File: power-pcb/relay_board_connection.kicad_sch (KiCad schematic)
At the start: 17 parts, among them J1 RA25S

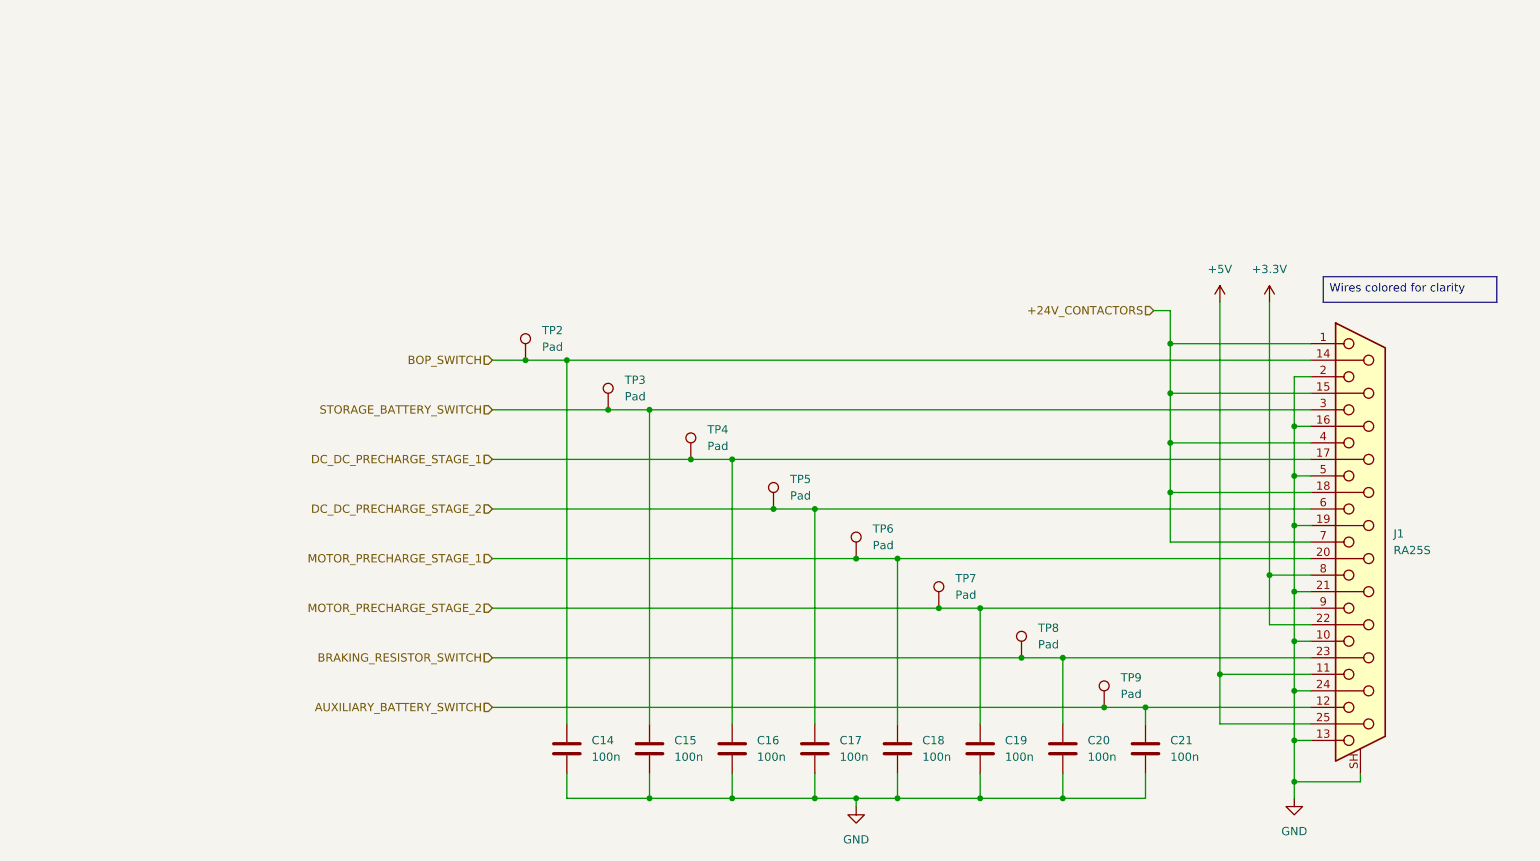
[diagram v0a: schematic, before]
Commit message: power-pcb: finish schematic pages 1 to 7
- overview
- non-isolated interfaces + power
- stm32 microcontroller
- relay board connection
- battery sensors
- 48v i-v sensing (x2)
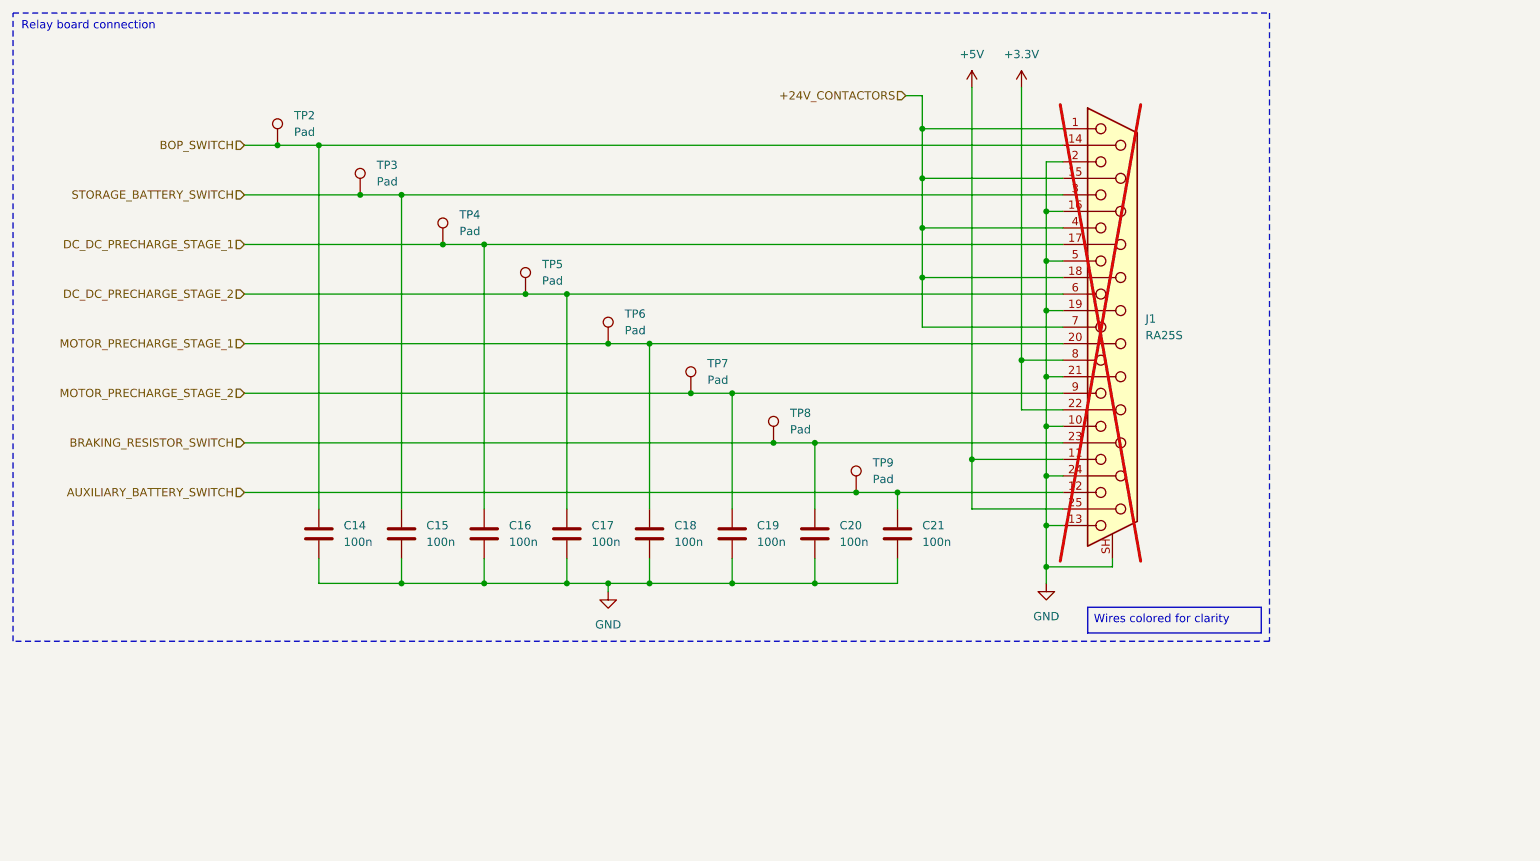
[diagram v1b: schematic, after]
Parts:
- J1: now not fitted
- TP2, TP3, TP4, TP5, TP6, TP7, TP8, TP9: now left out of the parts list
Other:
- note added: "Relay board connection"
- moved on the sheet: C14, C15, C16, C17, C18, C19, C20, C21, TP2, TP3, TP4, TP5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

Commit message: power-pcb: finish schematic layout
All parts are placed and connected, ERC passes (except for two
exclusions with comment).
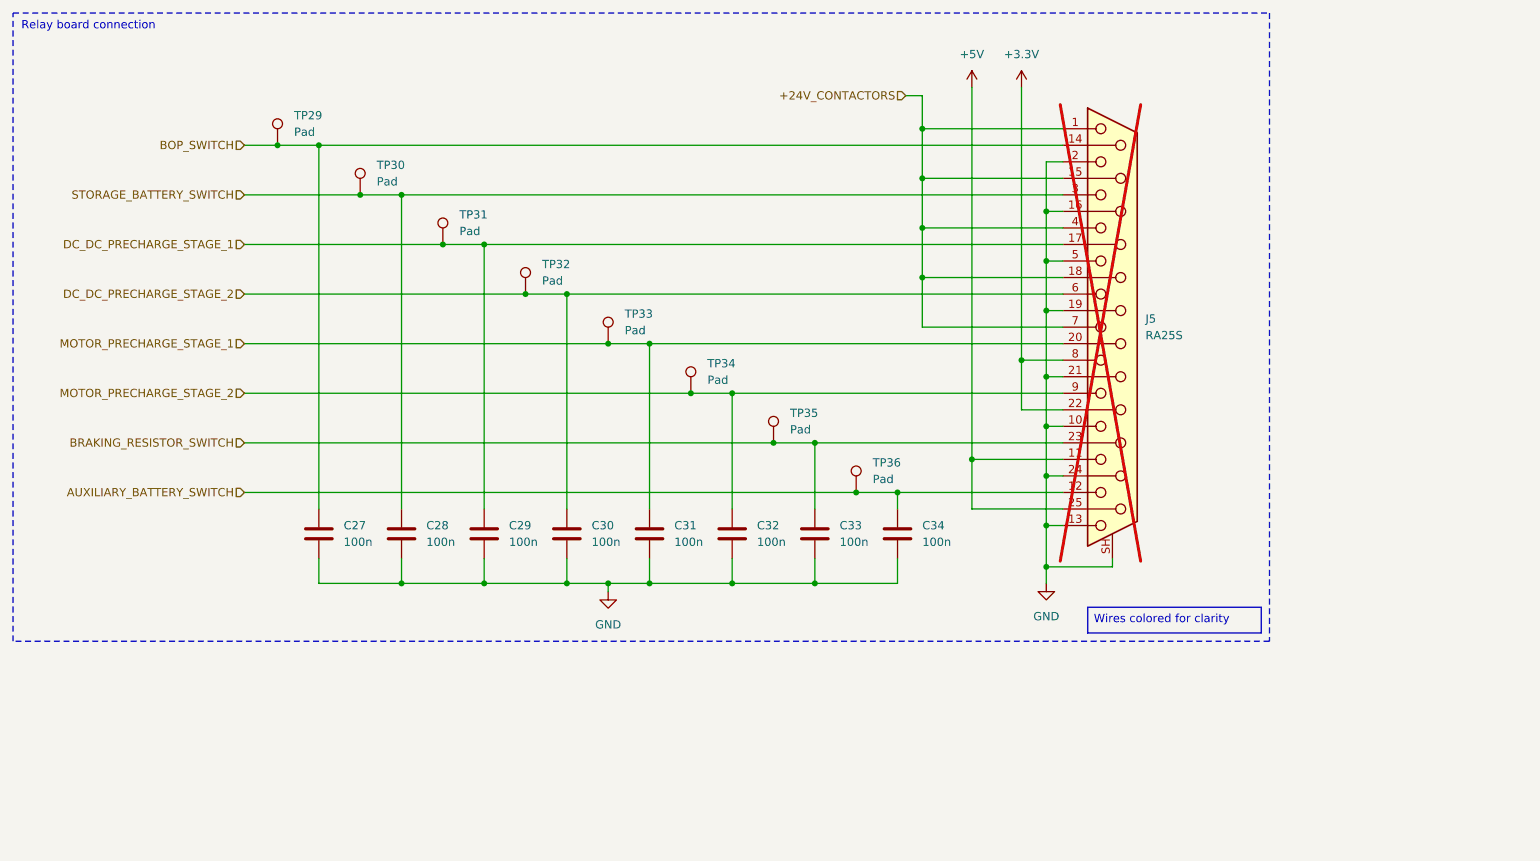
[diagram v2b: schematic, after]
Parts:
- renumbered C14 to C27, C15 to C28, C16 to C29, C17 to C30, C18 to C31, C19 to C32, C20 to C33, C21 to C34, J1 to J5, TP2 to TP29, TP3 to TP30, TP4 to TP31, TP5 to TP32, TP6 to TP33, TP7 to TP34, TP8 to TP35, TP9 to TP36
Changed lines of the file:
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@@
 	(title_block
 		(title "Relay Board Connection")
-		(date "2026-05-31")
+		(date "2026-06-13")
 		(rev "v1.1.0")
 	)
@@
 		(dnp no)
 		(fields_autoplaced yes)
-		(property "Reference" "C20"
+		(property "Reference" "C33"
 			(at 139.7 91.4399 0)
 			(show_name no)
@@
 			(project "power-pcb"
 				(path "/4b4cf3aa-c94c-4150-b9c5-35049cd71136/9838bcc9-e766-495a-ad52-0ec70b90713f"
-					(reference "C20")
+					(reference "C33")
 					(unit 1)
+					(variant
+						(name "JLCPCB")
+					)
 				)
 			)
@@
 		(dnp no)
 		(fields_autoplaced yes)
-		(property "Reference" "C16"
+		(property "Reference" "C29"
 			(at 88.9 91.4399 0)
 			(show_name no)
@@
 			(project "power-pcb"
 				(path "/4b4cf3aa-c94c-4150-b9c5-35049cd71136/9838bcc9-e766-495a-ad52-0ec70b90713f"
-					(reference "C16")
+					(reference "C29")
 					(unit 1)
+					(variant
+						(name "JLCPCB")
+					)
 				)
 			)
@@
 		(dnp no)
 		(fields_autoplaced yes)
-		(property "Reference" "#PWR020"
+		(property "Reference" "#PWR058"
 			(at 104.14 107.95 0)
 			(hide yes)
@@
 			(project "power-pcb"
 				(path "/4b4cf3aa-c94c-4150-b9c5-35049cd71136/9838bcc9-e766-495a-ad52-0ec70b90713f"
-					(reference "#PWR020")
+					(reference "#PWR058")
 					(unit 1)
 				)
@@
 		(dnp no)
 		(fields_autoplaced yes)
-		(property "Reference" "TP3"
+		(property "Reference" "TP30"
 			(at 68.58 36.0679 0)
 			(show_name no)
@@
 			(project "power-pcb"
 				(path "/4b4cf3aa-c94c-4150-b9c5-35049cd71136/9838bcc9-e766-495a-ad52-0ec70b90713f"
-					(reference "TP3")
+					(reference "TP30")
 					(unit 1)
+					(variant
+						(name "JLCPCB")
+					)
 				)
 			)
@@
 		(dnp no)
 		(fields_autoplaced yes)
-		(property "Reference" "C17"
+		(property "Reference" "C30"
 			(at 101.6 91.4399 0)
 			(show_name no)
@@
 			(project "power-pcb"
 				(path "/4b4cf3aa-c94c-4150-b9c5-35049cd71136/9838bcc9-e766-495a-ad52-0ec70b90713f"
-					(reference "C17")
+					(reference "C30")
 					(unit 1)
+					(variant
+						(name "JLCPCB")
+					)
 				)
 			)
@@
 		(dnp no)
 		(fields_autoplaced yes)
-		(property "Reference" "#PWR023"
+		(property "Reference" "#PWR057"
 			(at 171.45 106.68 0)
 			(hide yes)
@@
 			(project "power-pcb"
 				(path "/4b4cf3aa-c94c-4150-b9c5-35049cd71136/9838bcc9-e766-495a-ad52-0ec70b90713f"
-					(reference "#PWR023")
+					(reference "#PWR057")
 					(unit 1)
 				)
@@
 		(dnp no)
 		(fields_autoplaced yes)
-		(property "Reference" "TP2"
+		(property "Reference" "TP29"
 			(at 55.88 28.4479 0)
 			(show_name no)
@@
 			(project "power-pcb"
 				(path "/4b4cf3aa-c94c-4150-b9c5-35049cd71136/9838bcc9-e766-495a-ad52-0ec70b90713f"
-					(reference "TP2")
+					(reference "TP29")
 					(unit 1)
+					(variant
+						(name "JLCPCB")
+					)
 				)
 			)
@@
 		(dnp no)
 		(fields_autoplaced yes)
-		(property "Reference" "TP9"
+		(property "Reference" "TP36"
 			(at 144.78 81.7879 0)
 			(show_name no)
@@
 			(project "power-pcb"
 				(path "/4b4cf3aa-c94c-4150-b9c5-35049cd71136/9838bcc9-e766-495a-ad52-0ec70b90713f"
-					(reference "TP9")
+					(reference "TP36")
 					(unit 1)
+					(variant
+						(name "JLCPCB")
+					)
 				)
 			)
@@
 		(dnp yes)
 		(fields_autoplaced yes)
-		(property "Reference" "J1"
+		(property "Reference" "J5"
 			(at 186.69 59.6899 0)
 			(show_name no)
@@
 			(project "power-pcb"
 				(path "/4b4cf3aa-c94c-4150-b9c5-35049cd71136/9838bcc9-e766-495a-ad52-0ec70b90713f"
-					(reference "J1")
+					(reference "J5")
 					(unit 1)
+					(variant
+						(name "JLCPCB")
+					)
 				)
 			)
@@
 		(dnp no)
 		(fields_autoplaced yes)
-		(property "Reference" "#PWR021"
+		(property "Reference" "#PWR055"
 			(at 160.02 27.94 0)
 			(hide yes)
@@
 			(project "power-pcb"
 				(path "/4b4cf3aa-c94c-4150-b9c5-35049cd71136/9838bcc9-e766-495a-ad52-0ec70b90713f"
-					(reference "#PWR021")
+					(reference "#PWR055")
 					(unit 1)
 				)
@@
 		(dnp no)
 		(fields_autoplaced yes)
-		(property "Reference" "#PWR022"
+		(property "Reference" "#PWR056"
 			(at 167.64 27.94 0)
 			(hide yes)
@@
 			(project "power-pcb"
 				(path "/4b4cf3aa-c94c-4150-b9c5-35049cd71136/9838bcc9-e766-495a-ad52-0ec70b90713f"
-					(reference "#PWR022")
+					(reference "#PWR056")
 					(unit 1)
 				)
@@
 		(dnp no)
 		(fields_autoplaced yes)
-		(property "Reference" "TP8"
+		(property "Reference" "TP35"
 			(at 132.08 74.1679 0)
 			(show_name no)
@@
 			(project "power-pcb"
 				(path "/4b4cf3aa-c94c-4150-b9c5-35049cd71136/9838bcc9-e766-495a-ad52-0ec70b90713f"
-					(reference "TP8")
+					(reference "TP35")
 					(unit 1)
+					(variant
+						(name "JLCPCB")
+					)
 				)
 			)
@@
 		(dnp no)
 		(fields_autoplaced yes)
-		(property "Reference" "C21"
+		(property "Reference" "C34"
 			(at 152.4 91.4399 0)
 			(show_name no)
@@
 			(project "power-pcb"
 				(path "/4b4cf3aa-c94c-4150-b9c5-35049cd71136/9838bcc9-e766-495a-ad52-0ec70b90713f"
-					(reference "C21")
+					(reference "C34")
 					(unit 1)
+					(variant
+						(name "JLCPCB")
+					)
 				)
 			)
@@
 		(dnp no)
 		(fields_autoplaced yes)
-		(property "Reference" "TP6"
+		(property "Reference" "TP33"
 			(at 106.68 58.9279 0)
 			(show_name no)
@@
 			(project "power-pcb"
 				(path "/4b4cf3aa-c94c-4150-b9c5-35049cd71136/9838bcc9-e766-495a-ad52-0ec70b90713f"
-					(reference "TP6")
+					(reference "TP33")
 					(unit 1)
+					(variant
+						(name "JLCPCB")
+					)
 				)
 			)
@@
 		(dnp no)
 		(fields_autoplaced yes)
-		(property "Reference" "TP5"
+		(property "Reference" "TP32"
 			(at 93.98 51.3079 0)
 			(show_name no)
@@
 			(project "power-pcb"
 				(path "/4b4cf3aa-c94c-4150-b9c5-35049cd71136/9838bcc9-e766-495a-ad52-0ec70b90713f"
-					(reference "TP5")
+					(reference "TP32")
 					(unit 1)
+					(variant
+						(name "JLCPCB")
+					)
 				)
 			)
@@
 		(dnp no)
 		(fields_autoplaced yes)
-		(property "Reference" "C18"
+		(property "Reference" "C31"
 			(at 114.3 91.4399 0)
 			(show_name no)
@@
 			(project "power-pcb"
 				(path "/4b4cf3aa-c94c-4150-b9c5-35049cd71136/9838bcc9-e766-495a-ad52-0ec70b90713f"
-					(reference "C18")
+					(reference "C31")
 					(unit 1)
+					(variant
+						(name "JLCPCB")
+					)
 				)
 			)
@@
 		(dnp no)
 		(fields_autoplaced yes)
-		(property "Reference" "C19"
+		(property "Reference" "C32"
 			(at 127 91.4399 0)
 			(show_name no)
@@
 			(project "power-pcb"
 				(path "/4b4cf3aa-c94c-4150-b9c5-35049cd71136/9838bcc9-e766-495a-ad52-0ec70b90713f"
-					(reference "C19")
+					(reference "C32")
 					(unit 1)
+					(variant
+						(name "JLCPCB")
+					)
 				)
 			)
@@
 		(dnp no)
 		(fields_autoplaced yes)
-		(property "Reference" "TP7"
+		(property "Reference" "TP34"
 			(at 119.38 66.5479 0)
 			(show_name no)
@@
 			(project "power-pcb"
 				(path "/4b4cf3aa-c94c-4150-b9c5-35049cd71136/9838bcc9-e766-495a-ad52-0ec70b90713f"
-					(reference "TP7")
+					(reference "TP34")
 					(unit 1)
+					(variant
+						(name "JLCPCB")
+					)
 				)
 			)
@@
 		(dnp no)
 		(fields_autoplaced yes)
-		(property "Reference" "C15"
+		(property "Reference" "C28"
 			(at 76.2 91.4399 0)
 			(show_name no)
@@
 			(project "power-pcb"
 				(path "/4b4cf3aa-c94c-4150-b9c5-35049cd71136/9838bcc9-e766-495a-ad52-0ec70b90713f"
-					(reference "C15")
+					(reference "C28")
 					(unit 1)
+					(variant
+						(name "JLCPCB")
+					)
 				)
 			)
@@
 		(dnp no)
 		(fields_autoplaced yes)
-		(property "Reference" "TP4"
+		(property "Reference" "TP31"
 			(at 81.28 43.6879 0)
 			(show_name no)
@@
 			(project "power-pcb"
 				(path "/4b4cf3aa-c94c-4150-b9c5-35049cd71136/9838bcc9-e766-495a-ad52-0ec70b90713f"
-					(reference "TP4")
+					(reference "TP31")
 					(unit 1)
+					(variant
+						(name "JLCPCB")
+					)
 				)
 			)
@@
 		(dnp no)
 		(fields_autoplaced yes)
-		(property "Reference" "C14"
+		(property "Reference" "C27"
 			(at 63.5 91.4399 0)
 			(show_name no)
@@
 			(project "power-pcb"
 				(path "/4b4cf3aa-c94c-4150-b9c5-35049cd71136/9838bcc9-e766-495a-ad52-0ec70b90713f"
-					(reference "C14")
+					(reference "C27")
 					(unit 1)
-				)
-			)
+					(variant
+						(name "JLCPCB")
+					)
+				)
+			)

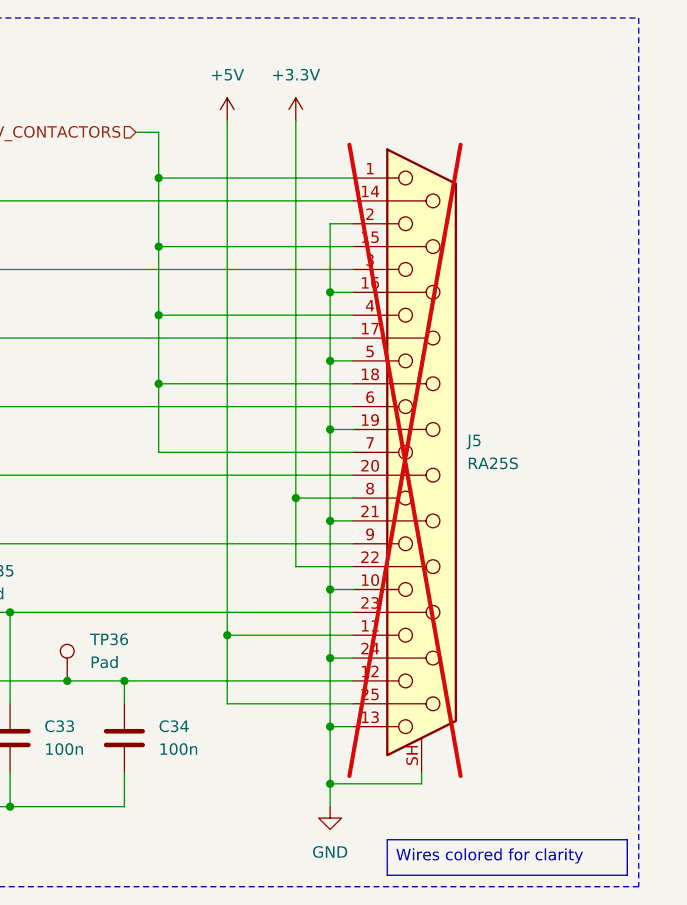
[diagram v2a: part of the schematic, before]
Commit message: power-pcb: finish assigning JLCPCB PN
Also assigned missing footprints.
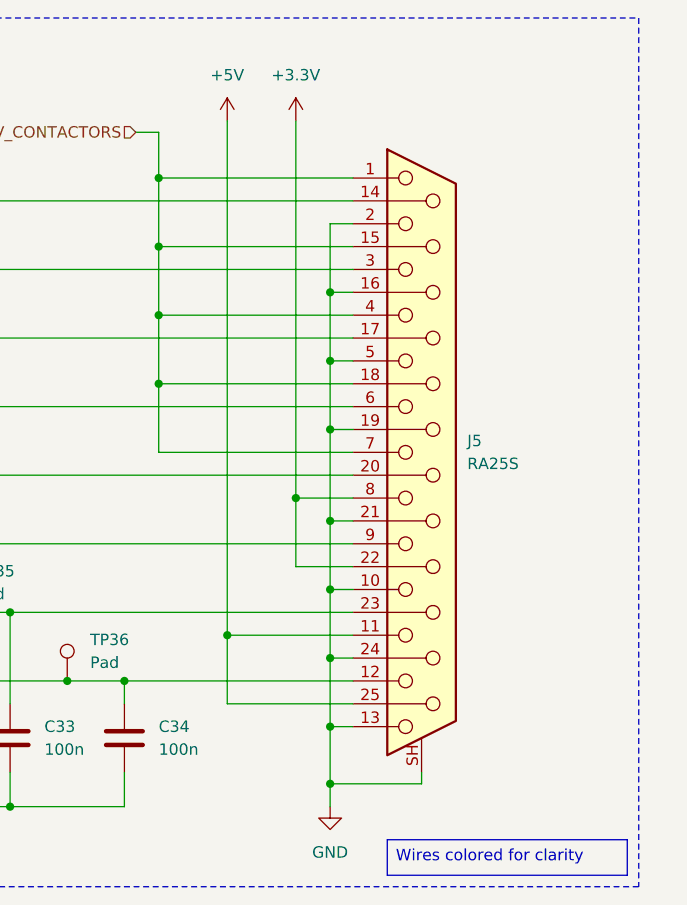
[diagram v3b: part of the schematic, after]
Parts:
- J5: MFR (none) -> Assmann WSW Components; MPN (none) -> A-DF 25 A/KG-T2S; now fitted
- TP29, TP30, TP31, TP32, TP33, TP34, TP35, TP36: footprint (none) -> TestPoint:TestPoint_Pad_D1.5mm
